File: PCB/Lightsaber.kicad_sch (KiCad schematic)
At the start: 44 parts

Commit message: resume project
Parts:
- L?: renamed from ?; value L -> 170µ
- R?: renamed from ?; value R -> 10K
- R?: renamed from ?; value 10K -> 15K
- R?: renamed from ?; value 27K -> 47K
- gave numbers to parts that had none: 24
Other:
- note added: "R1"
- note added: "R2"
- note added: "Vout = 1.25+1.25*(R2/R1)"

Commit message: MCU connections added
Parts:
- added C2, C3: 1µ, symbol Device:C
- added C4, C5: 0.1µ, symbol Device:C
- added J1: Conn_01x03_Socket, symbol Connector:Conn_01x03_Socket
- added R7, R8: 4.7K, Resistor_SMD:R_0402_1005Metric, symbol Device:R
- added U2: ATtiny1616-M, Package_DFN_QFN:VQFN-20-1EP_3x3mm_P0.4mm_EP1.7x1.7mm, symbol MCU_Microchip_ATtiny:ATtiny1616-M
- added U3: ~, symbol Lightsaber_custom:MC3479
- added U4: MIC5504-3.3YM5, Package_TO_SOT_SMD:SOT-23-5, symbol Regulator_Linear:MIC5504-3.3YM5
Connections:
- net +5V: now also C3.1, C5.1, J1.1 (Pin_1), U2.4 (VCC), U4.1 (VIN)
- net AUDIO: now also U2.7 (PA6)
- net B: now also U2.10 (PB4)
- net BTN_LED: now also U2.11 (PB3)
- net G: now also U2.9 (PB5)
- net GND: now also C2.2, C3.2, C4.2, C5.2, J1.3 (Pin_3), U2.21 (GND), U2.3 (GND), U3.6 (GND), U3.7 (VPP), U4.2 (GND)
- net R: now also U2.8 (PA7)
- net SHD_CONTROL: now also U2.6 (PA5)
- net BTN_SENS renamed BTN_INT
- net BTN_INT: now also U2.12 (PB2)
- new net +3.3V: C2.1, C4.1, R7.2, R8.2, U3.9 (VDD), U4.5 (VOUT)
- new net 3V3 EN: U2.15 (PC0), U4.3 (EN)
- new net ACCEL_CSN: U2.5 (PA4), U3.2 (CSN)
- new net ACCEL_INT1: R7.1, U2.17 (PC2), U3.12 (INTN1)
- new net ACCEL_INT2: R8.1, U2.18 (PC3), U3.11 (INTN2)
- new net MISO: U2.1 (PA2), U2.20 (PA1), U3.3 (DOUT_A6)
- new net MOSI: U3.4 (DIN_SDA)
- new net SCK: U2.2 (PA3), U3.1 (SCK_SCL)
- new net UDPI: J1.2 (Pin_2), U2.19 (~{RESET}/PA0)
- no-connect marks 1 -> 7

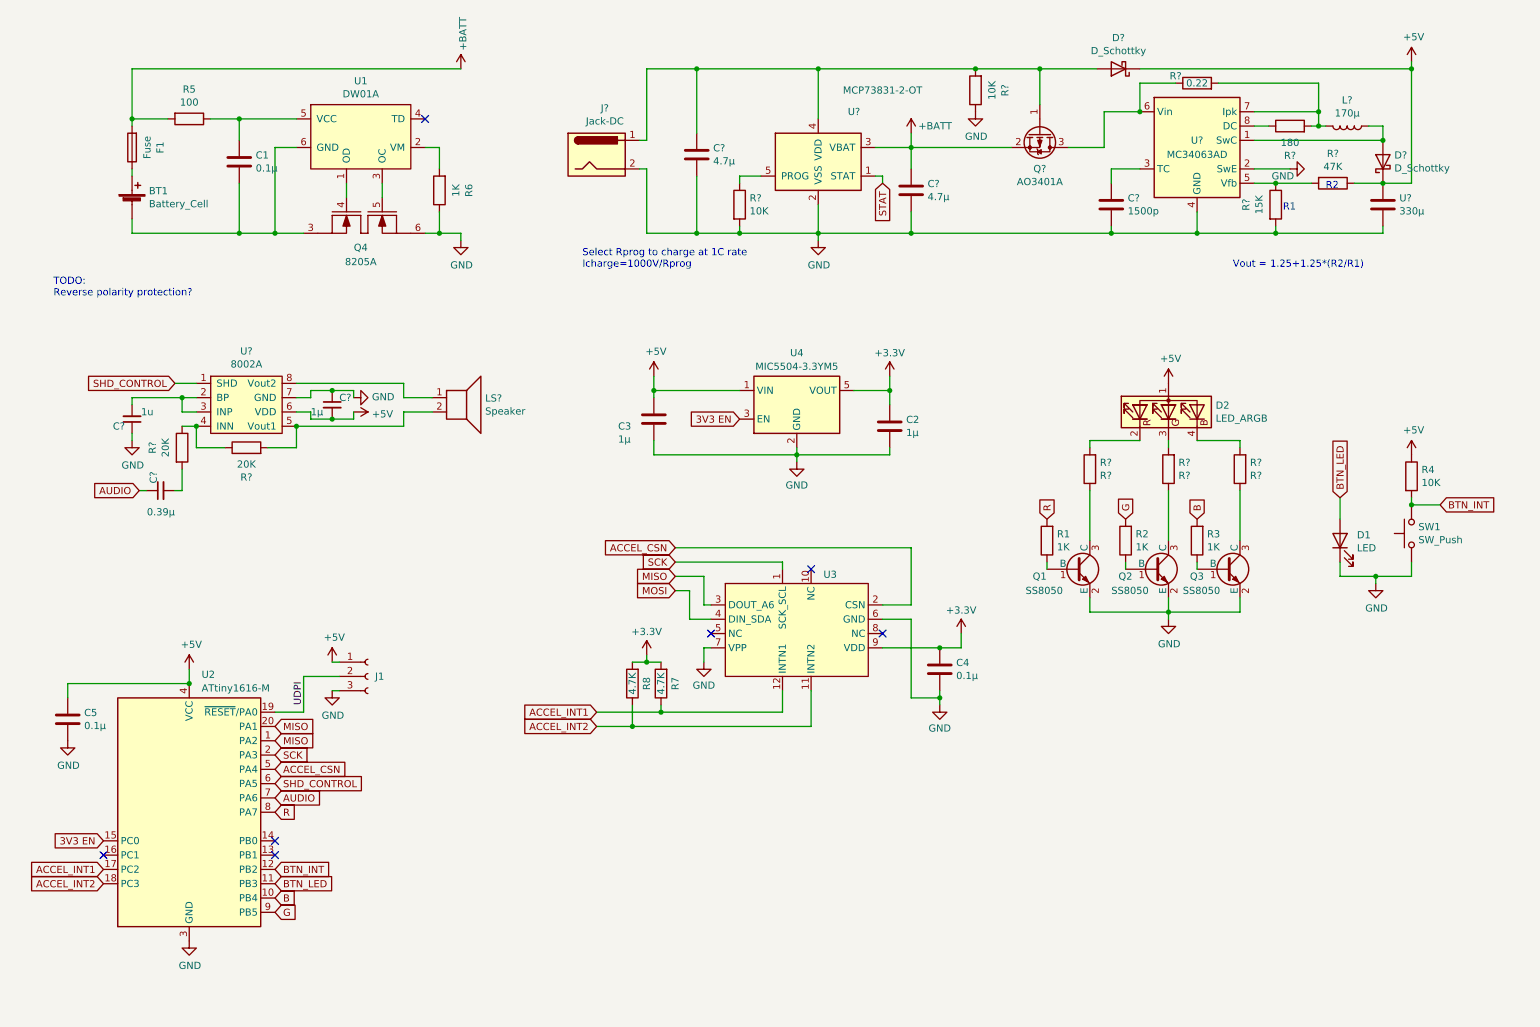
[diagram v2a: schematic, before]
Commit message: added filter for audio
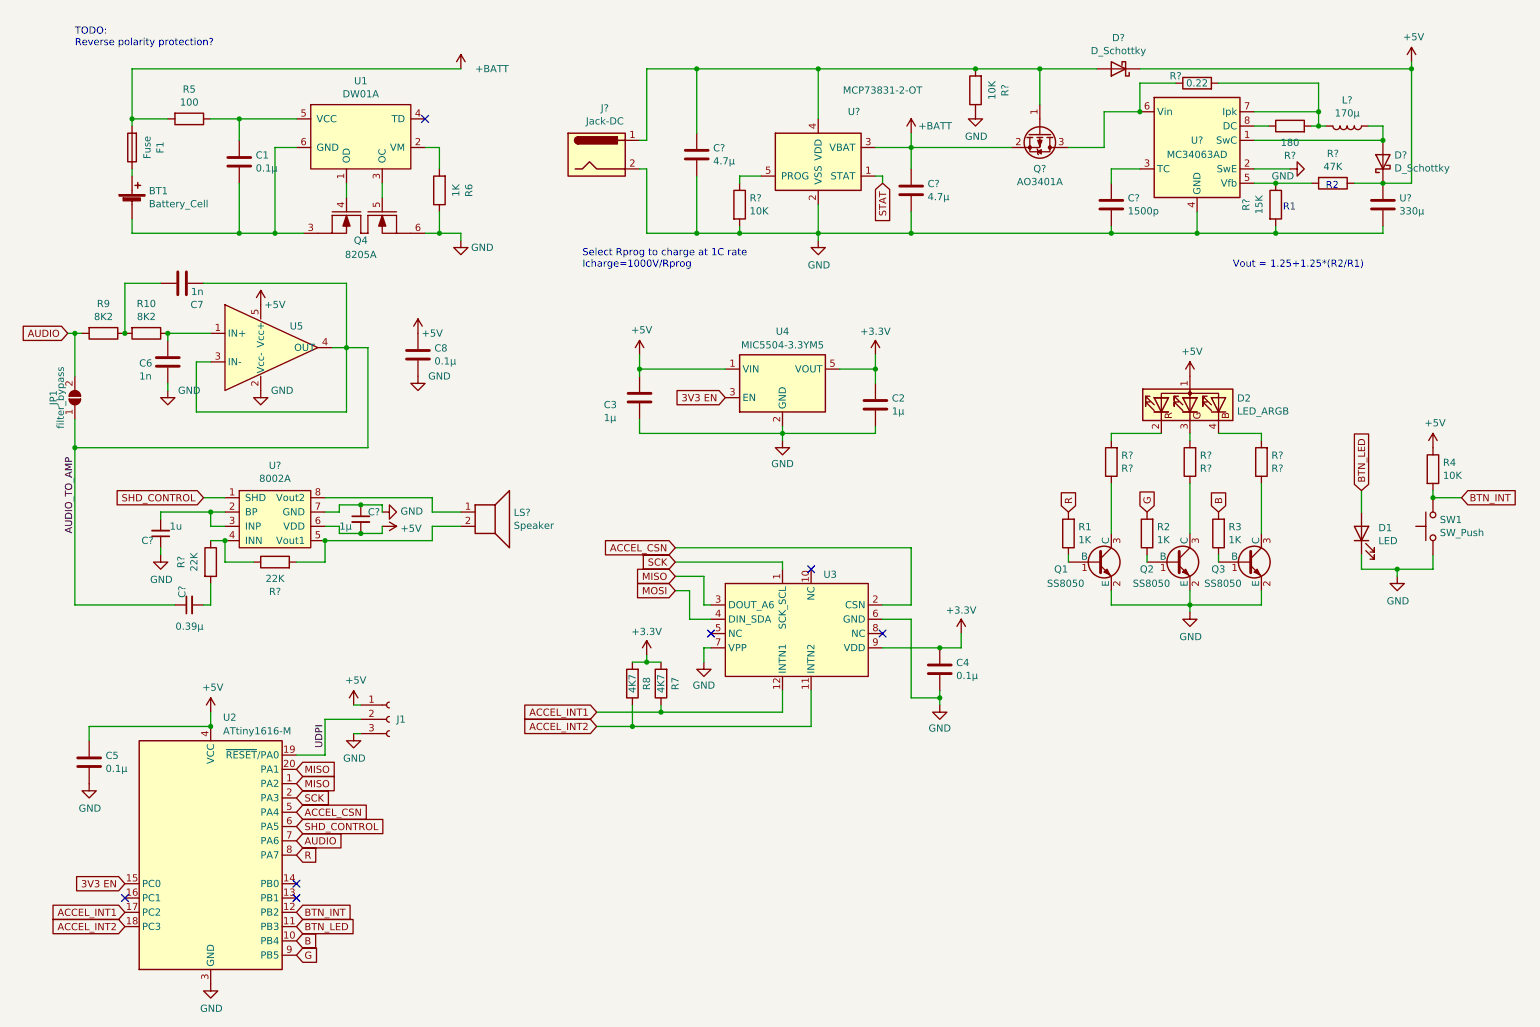
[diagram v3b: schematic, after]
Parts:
- added C6, C7: 1n, symbol Device:C
- added C8: 0.1µ, symbol Device:C
- added JP1: filter_bypass, symbol Jumper:SolderJumper_2_Open
- added R10, R9: 8K2, Resistor_SMD:R_0402_1005Metric, symbol Device:R
- added U5: ~, symbol Lightsaber_custom:TSV611
- R7, R8: value 4.7K -> 4K7
- R? (x2): value 20K -> 22K
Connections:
- net +5V: now also C8.1, U5.5 (Vcc+)
- net AUDIO: now also JP1.2 (B), R9.2; no longer C?.1
- net GND: now also C6.2, C8.2, U5.2 (Vcc-)
- new net: C7.1, R10.2, R9.1
- new net: C6.1, R10.1, U5.1 (IN+)
- new net AUDIO_TO_AMP: C7.2, C?.1, JP1.1 (A), U5.3 (IN-), U5.4 (OUT)
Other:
- moved on the sheet: C2, C3, C5, C?, D1, D2, J1, LS?, Q1, Q2, Q3, R1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
